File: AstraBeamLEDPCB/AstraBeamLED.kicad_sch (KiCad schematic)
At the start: 0 parts

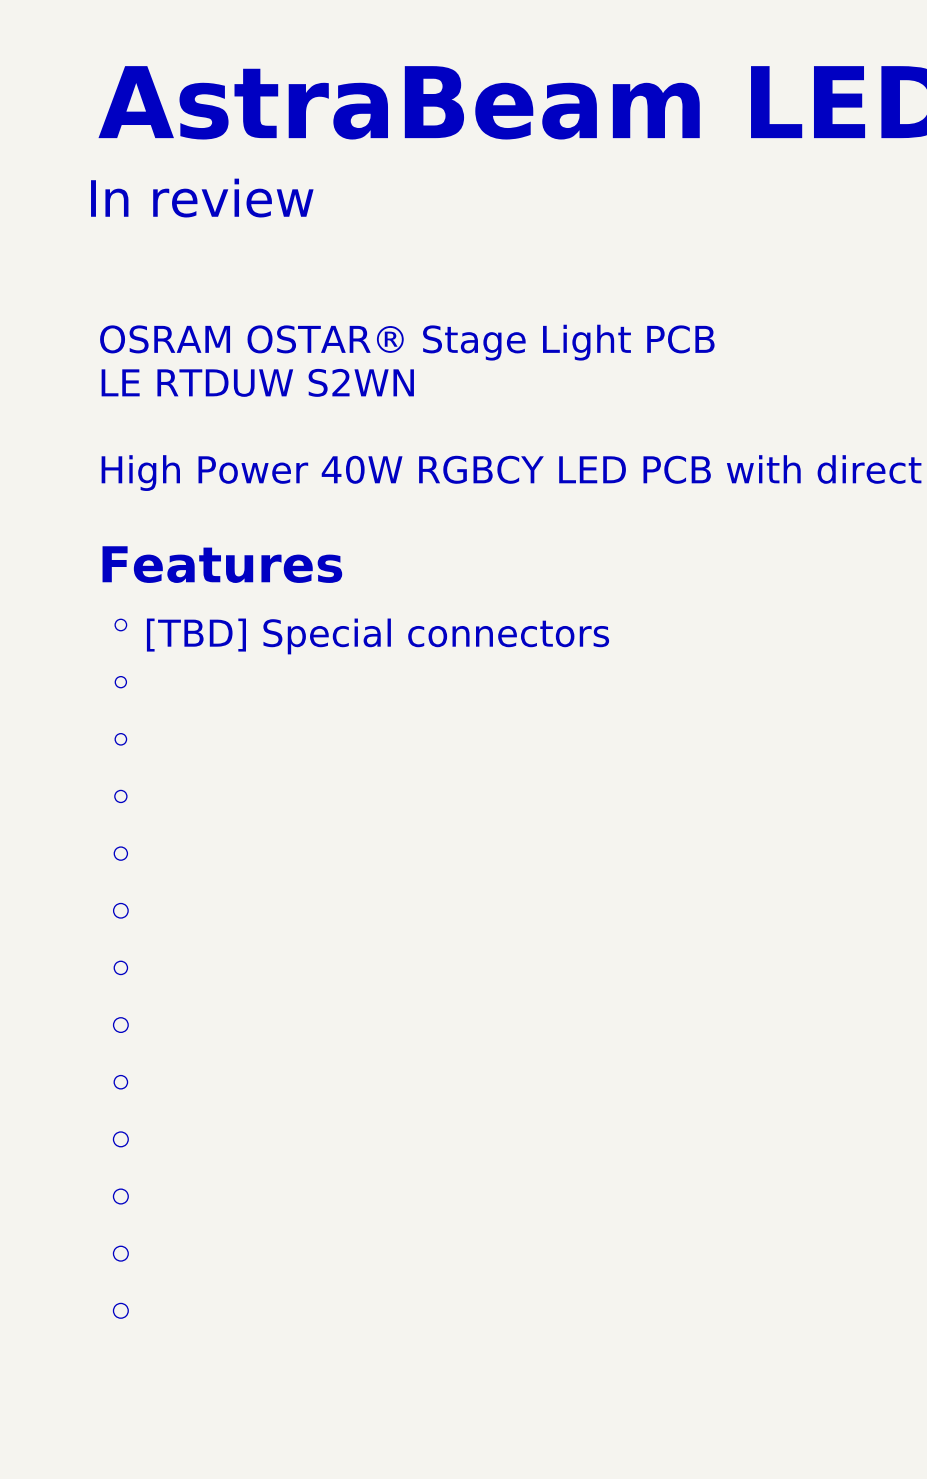
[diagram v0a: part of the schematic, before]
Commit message: Updated labels, description
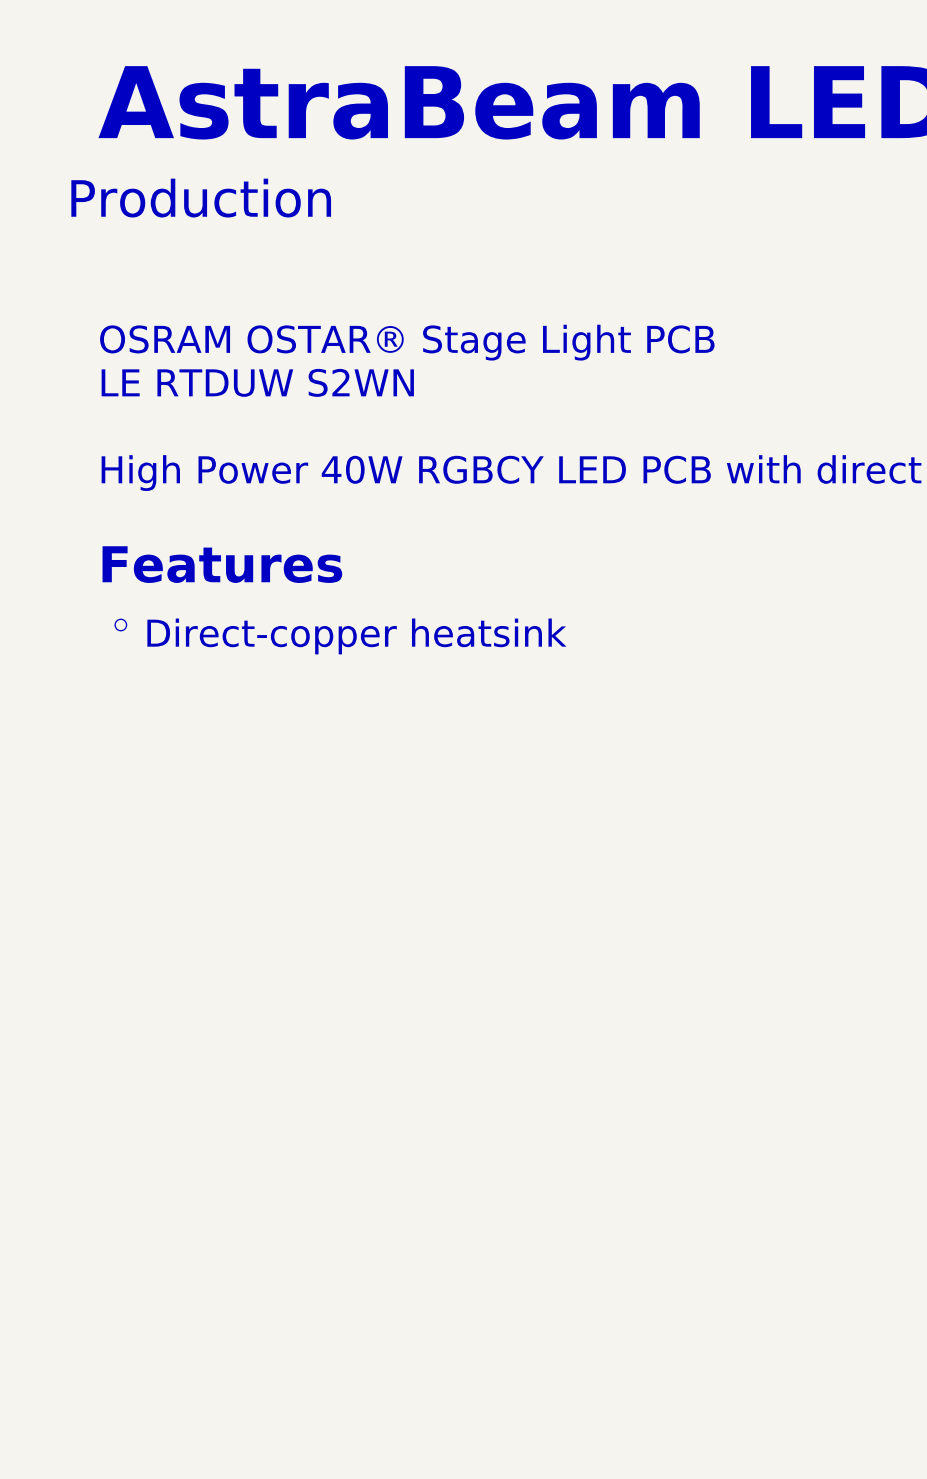
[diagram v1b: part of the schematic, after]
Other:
- note added: "Direct-copper heatsink"
- note added: "Production"
- note removed: "In review"
- note removed: "[TBD] Special connectors"
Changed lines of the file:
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@@
 		(company "LiveAstra Technologies")
-	)
-	(circle
-		(center 22.86 127)
-		(radius 0.7354)
-		(stroke
-			(width -0.0001)
-			(type default)
-		)
-		(fill
-			(type color)
-			(color 0 0 0 0)
-		)
-	)
-	(circle
-		(center 22.86 120.65)
-		(radius 0.807)
-		(stroke
-			(width -0.0001)
-			(type default)
-		)
-		(fill
-			(type color)
-			(color 0 0 0 0)
-		)
-	)
-	(circle
-		(center 22.86 114.3)
-		(radius 0.73)
-		(stroke
-			(width -0.0001)
-			(type default)
-		)
-		(fill
-			(type color)
-			(color 0 0 0 0)
-		)
-	)
-	(circle
-		(center 22.86 158.75)
-		(radius 0.82)
-		(stroke
-			(width -0.0001)
-			(type default)
-		)
-		(fill
-			(type color)
-			(color 0 0 0 0)
-		)
-	)
-	(circle
-		(center 22.86 133.35)
-		(radius 0.8135)
-		(stroke
-			(width -0.0001)
-			(type default)
-		)
-		(fill
-			(type color)
-			(color 0 0 0 0)
-		)
-	)
-	(circle
-		(center 22.86 152.4)
-		(radius 0.82)
-		(stroke
-			(width -0.0001)
-			(type default)
-		)
-		(fill
-			(type color)
-			(color 0 0 0 0)
-		)
-	)
-	(circle
-		(center 22.86 146.05)
-		(radius 0.82)
-		(stroke
-			(width -0.0001)
-			(type default)
-		)
-		(fill
-			(type color)
-			(color 0 0 0 0)
-		)
-	)
-	(circle
-		(center 22.86 101.6)
-		(radius 0.6306)
-		(stroke
-			(width -0.0001)
-			(type default)
-		)
-		(fill
-			(type color)
-			(color 0 0 0 0)
-		)
 	)
 	(rectangle
@@
 	)
 	(circle
-		(center 22.86 107.95)
-		(radius 0.6696)
-		(stroke
-			(width -0.0001)
-			(type default)
-		)
-		(fill
-			(type color)
-			(color 0 0 0 0)
-		)
-	)
-	(circle
-		(center 22.86 139.7)
-		(radius 0.7409)
-		(stroke
-			(width -0.0001)
-			(type default)
-		)
-		(fill
-			(type color)
-			(color 0 0 0 0)
-		)
-	)
-	(circle
 		(center 22.86 88.9)
 		(radius 0.6351)
-		(stroke
-			(width -0.0001)
-			(type default)
-		)
-		(fill
-			(type color)
-			(color 0 0 0 0)
-		)
-	)
-	(circle
-		(center 22.86 165.1)
-		(radius 0.82)
-		(stroke
-			(width -0.0001)
-			(type default)
-		)
-		(fill
-			(type color)
-			(color 0 0 0 0)
-		)
-	)
-	(circle
-		(center 22.86 95.25)
-		(radius 0.6174)
 		(stroke
 			(width -0.0001)
@@
 		)
 	)
-	(text "[TBD] Special connectors"
+	(text "Direct-copper heatsink"
 		(exclude_from_sim no)
 		(at 25.4 90.17 0)
@@
 		)
 	)
-	(text "In review"
+	(text "Production"
 		(exclude_from_sim no)
 		(at 31.75 41.91 0)

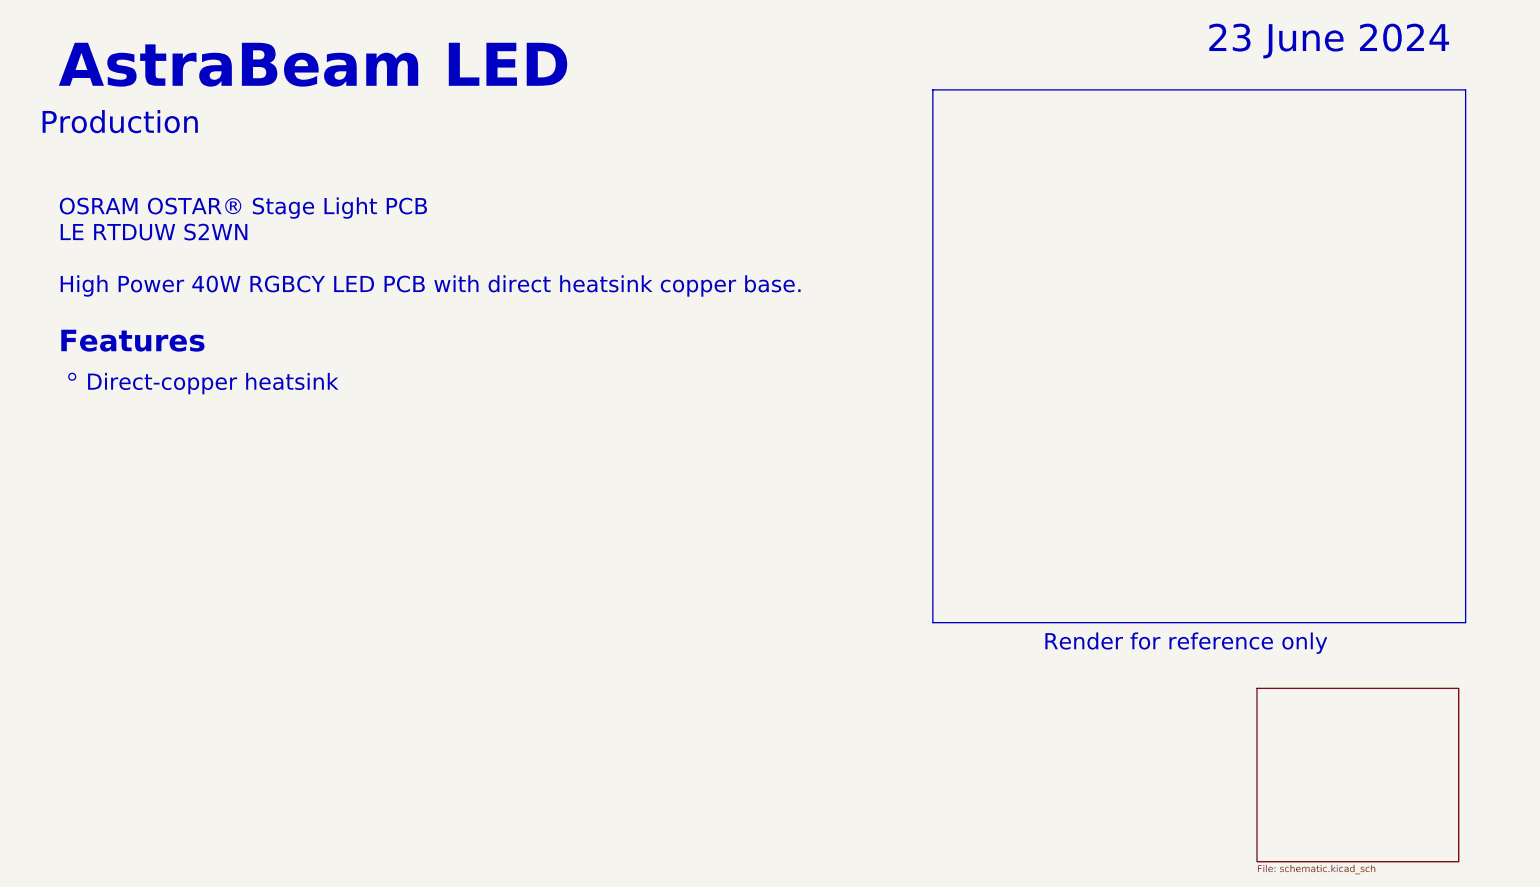
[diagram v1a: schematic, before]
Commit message: Updated datasheet render
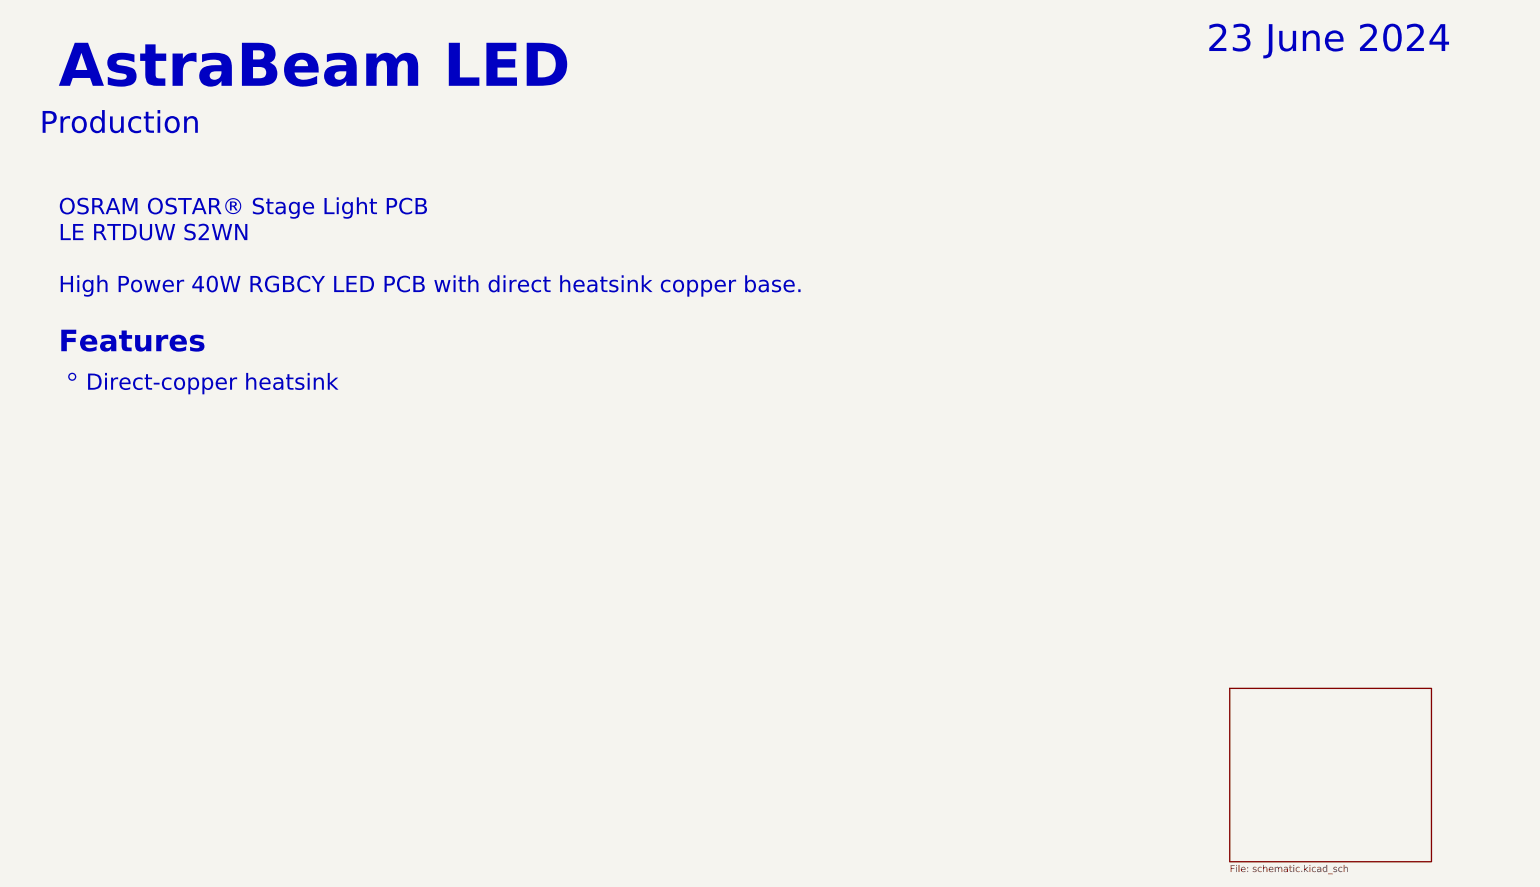
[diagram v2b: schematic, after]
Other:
- note removed: "Render for reference only"
